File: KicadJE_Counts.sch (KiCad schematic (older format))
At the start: 105 parts, among them J101 In7, J102 Doepfer connector, J104 In6, J105 In3, J106 Out10, J107 Out11, J108 Out9, J109 Out6, SW101 Dist 6, SW102 Crush A6, SW104 Rotary_Encoder_Switch, SW105 Dist 10, U101 TL072, U102 TL072

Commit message: counter fine
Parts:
- removed A101: Arduino_Nano_v3.x, Module:Arduino_Nano, symbol KicadJE_Counts-rescue:Arduino_Nano_v3.x-MCU_Module-Kicad_Counts-rescue
- removed C119: 100n, Capacitor_SMD:C_0805_2012Metric_Pad1.15x1.40mm_HandSolder, symbol Device:C_Small
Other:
- moved on the sheet: C104, C105, C106, C107, C108, C110, C111, C112, C114, C115, C116, C117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

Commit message: Update KicadJE_Counts.sch
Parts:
- removed C114: 47n, Capacitor_SMD:C_0805_2012Metric_Pad1.15x1.40mm_HandSolder, symbol Device:C
- removed C115, C116: 100n, Capacitor_SMD:C_0805_2012Metric_Pad1.15x1.40mm_HandSolder, symbol Device:C
- removed D103: LED1, LED_THT:LED_D3.0mm, symbol Device:LED
- removed D104: LED2, LED_THT:LED_D3.0mm, symbol Device:LED
- removed D105: LED3, LED_THT:LED_D3.0mm, symbol Device:LED
- removed D107: LED4, LED_THT:LED_D3.0mm, symbol Device:LED
- removed D109: LED_Out10, LED_THT:LED_D3.0mm, symbol Device:LED
- removed D112: LED_Out11, LED_THT:LED_D3.0mm, symbol Device:LED
- removed D113: LED_Out6, LED_THT:LED_D3.0mm, symbol Device:LED
- removed D114: LED_Out9, LED_THT:LED_D3.0mm, symbol Device:LED
- removed R106, R109, R110, R113, R114, R116, R118, R121: 680R, Resistor_SMD:R_0805_2012Metric_Pad1.15x1.40mm_HandSolder, symbol Device:R
- removed R125, R126, R127: 10k, Resistor_SMD:R_0805_2012Metric_Pad1.15x1.40mm_HandSolder, symbol Device:R
- removed SW104: Rotary_Encoder_Switch, Rotary_Encoder:RotaryEncoder_Alps_EC11E-Switch_Vertical_H20mm, symbol Device:Rotary_Encoder_Switch
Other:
- note removed: "Encoder Control"
- note removed: "LED Signals"
- moved on the sheet: C104, C105, C106, C107, C108, C110, C111, C112, C117, C120, C122, C123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

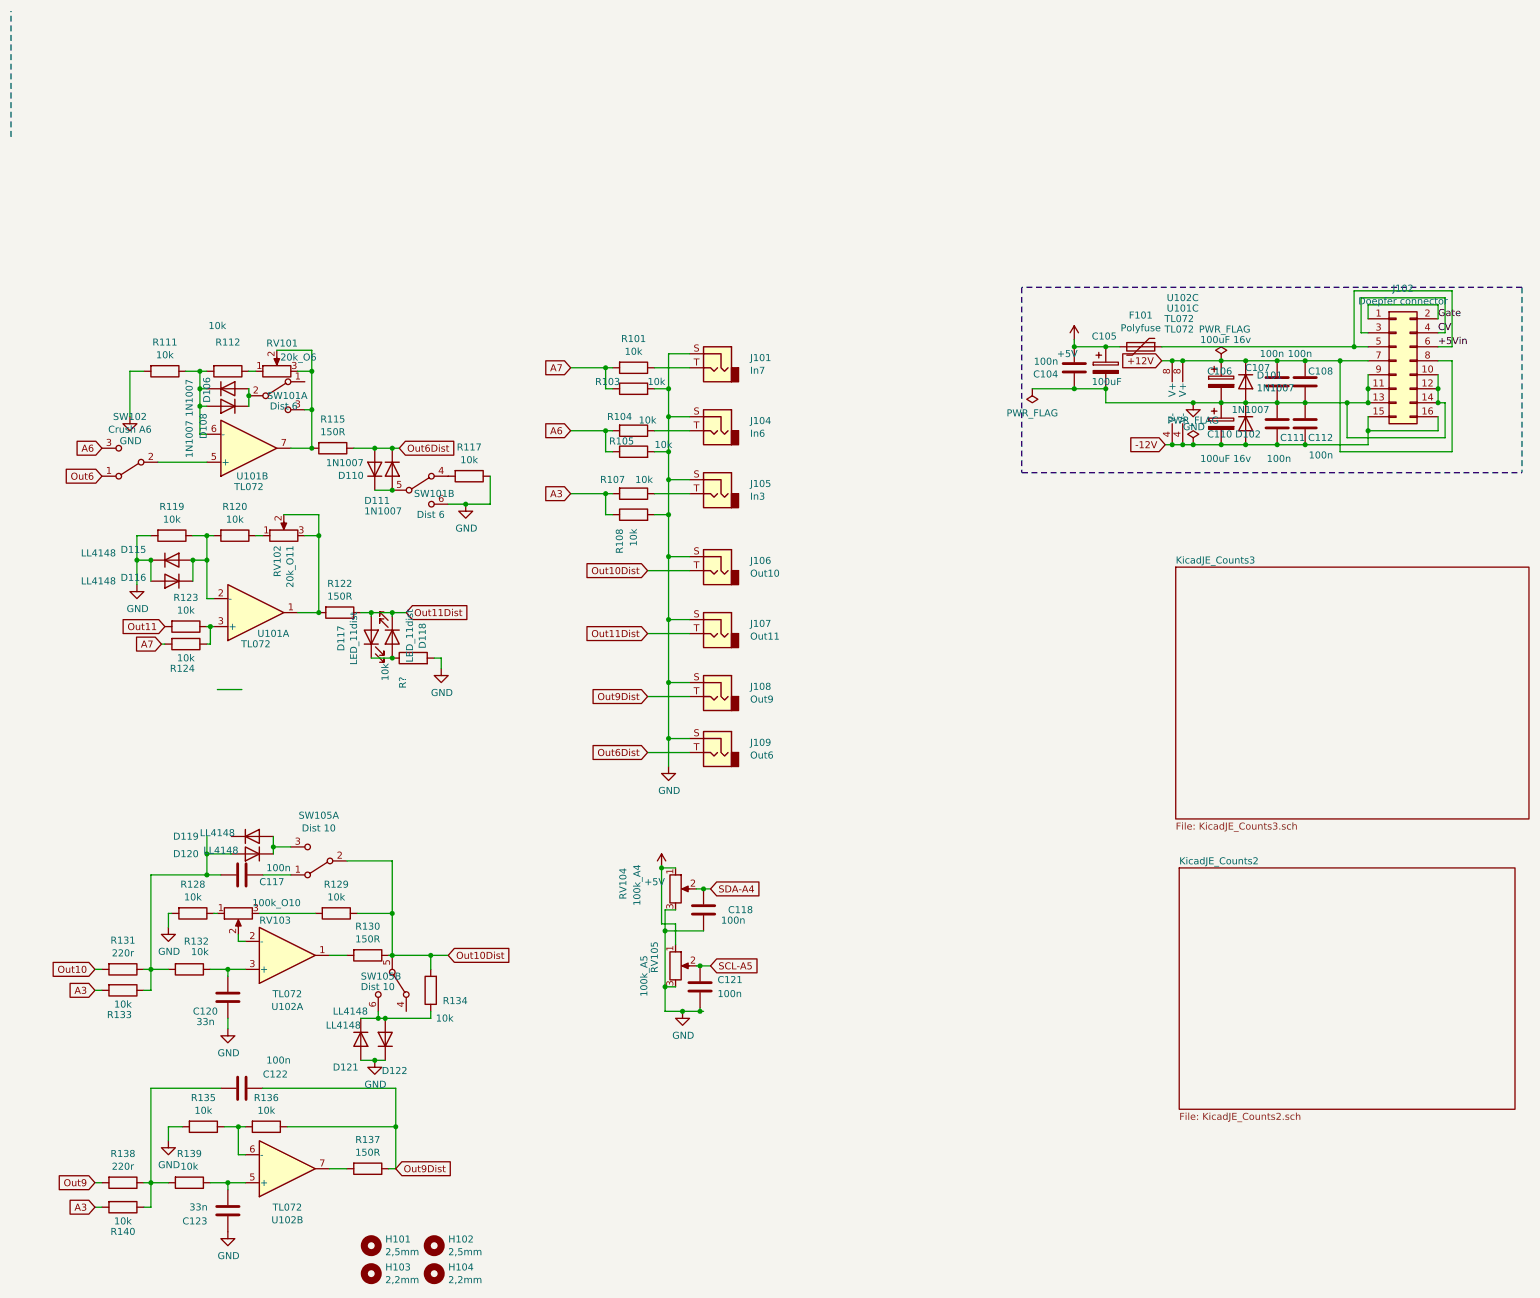
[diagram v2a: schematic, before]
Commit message: distortion added as count2
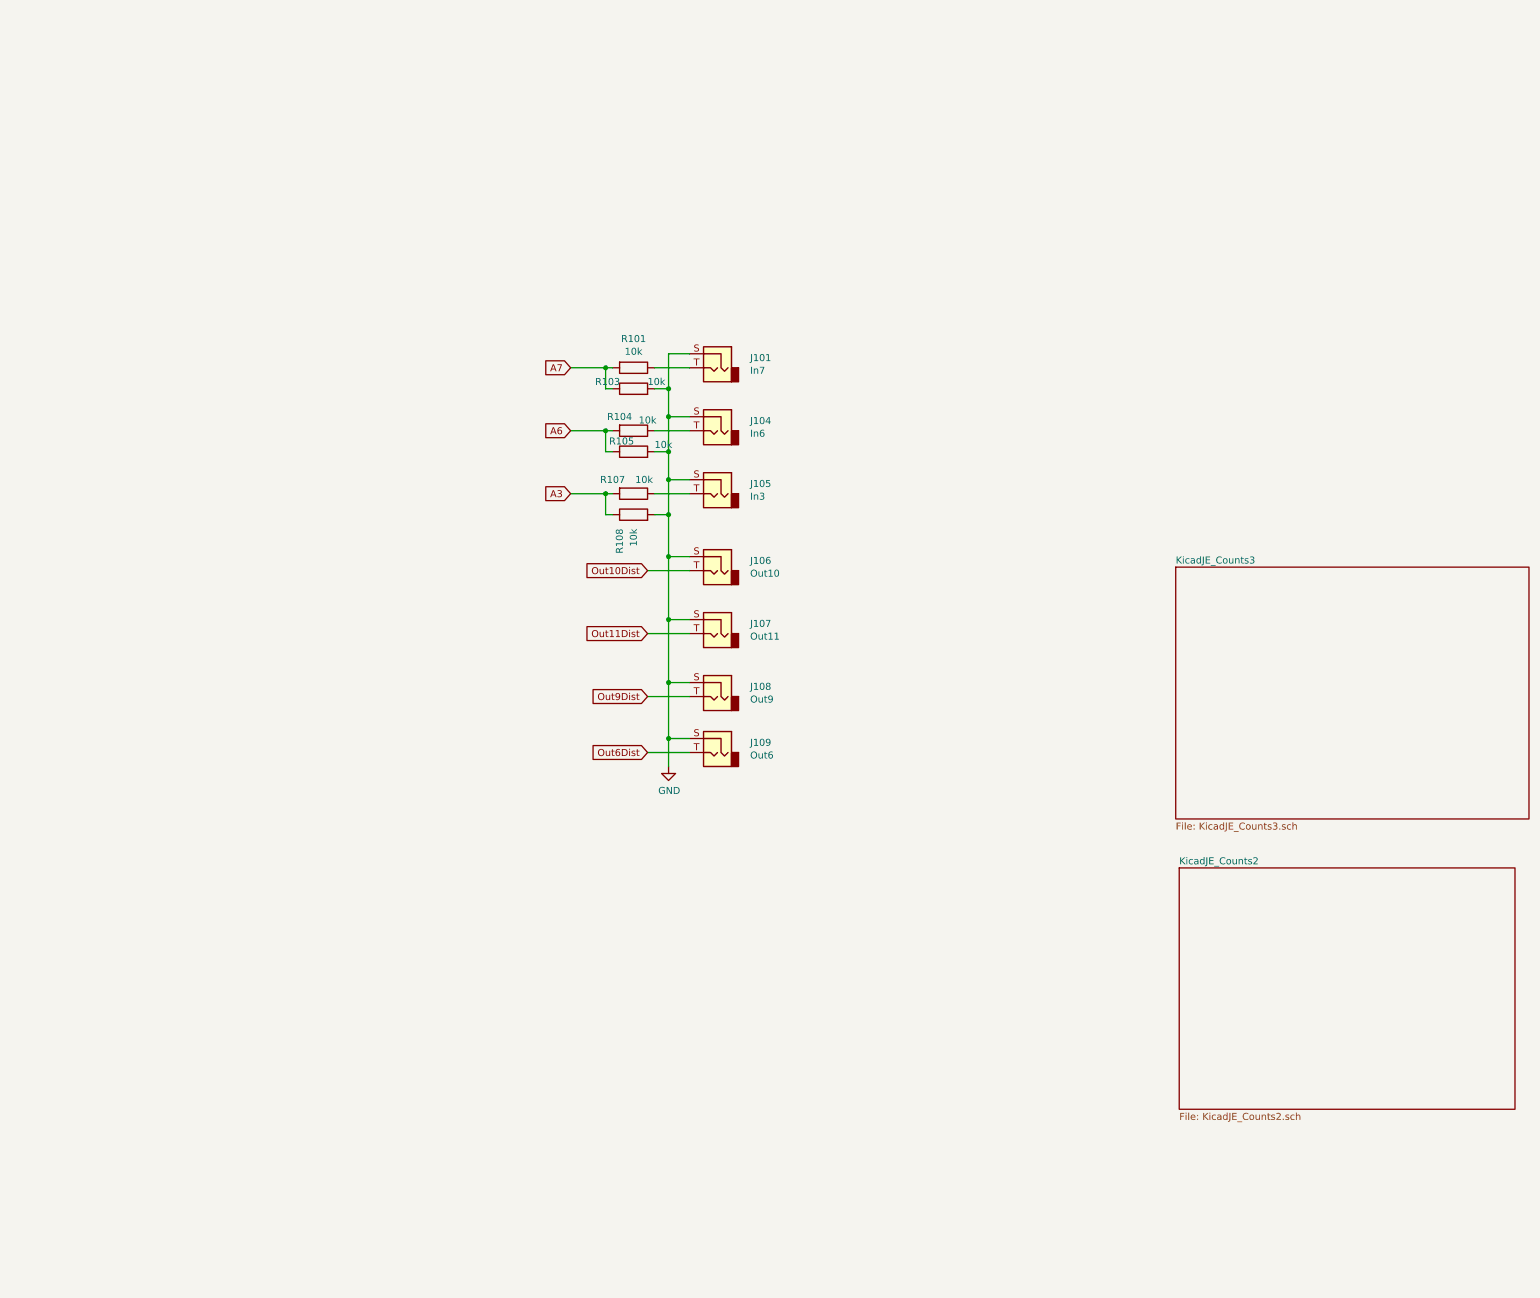
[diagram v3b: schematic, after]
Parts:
- removed C104, C107, C108, C111, C112, C117, C118, C121, C122: 100n, Capacitor_SMD:C_0805_2012Metric_Pad1.15x1.40mm_HandSolder, symbol Device:C
- removed C105: 100uF, Capacitor_THT:CP_Radial_D5.0mm_P2.50mm, symbol Device:CP
- removed C106, C110: 100uF 16v, Capacitor_THT:CP_Radial_D5.0mm_P2.50mm, symbol Device:CP
- removed C120, C123: 33n, Capacitor_SMD:C_0805_2012Metric_Pad1.15x1.40mm_HandSolder, symbol Device:C
- removed D101, D102, D106, D108: 1N1007, Diode_SMD:D_SOD-123, symbol Device:D
- removed D110, D111: 1N1007, Diode_SMD:D_0805_2012Metric_Pad1.15x1.40mm_HandSolder, symbol Device:D
- removed D115, D116, D119, D120, D121, D122: LL4148, Diode_SMD:D_MiniMELF, symbol Diode:LL4148
- removed D117: LED_11dist, LED_SMD:LED_0805_2012Metric_Pad1.15x1.40mm_HandSolder, symbol Device:LED
- removed D118: LED_11dist, Diode_SMD:D_0805_2012Metric_Pad1.15x1.40mm_HandSolder, symbol Device:LED
- removed F101: Polyfuse, Fuse:Fuse_1206_3216Metric_Pad1.42x1.75mm_HandSolder, symbol Device:Polyfuse
- removed H101, H102: 2,5mm, MountingHole:MountingHole_2.5mm_Pad_Via, symbol Mechanical:MountingHole
- removed H103: 2,2mm, MountingHole:MountingHole_2.5mm_Pad_Via, symbol Mechanical:MountingHole
- removed H104: 2,2mm, MountingHole:MountingHole_2.2mm_M2_Pad_Via, symbol Mechanical:MountingHole
- removed J102: Doepfer connector, Connector_PinSocket_2.54mm:PinSocket_2x08_P2.54mm_Vertical, symbol Connector_Generic:Conn_02x08_Odd_Even
- removed R111, R112, R117, R119, R120, R123, R124, R128, R129, R132, R133, R134, R135, R136, R139, R140, R?: 10k, Resistor_SMD:R_0805_2012Metric_Pad1.15x1.40mm_HandSolder, symbol Device:R
- removed R115, R122, R130, R137: 150R, Resistor_SMD:R_0805_2012Metric_Pad1.15x1.40mm_HandSolder, symbol Device:R
- removed R131, R138: 220r, Resistor_SMD:R_0805_2012Metric_Pad1.15x1.40mm_HandSolder, symbol Device:R
- removed RV101: 20k_O6, Potentiometer_THT:Potentiometer_China_RK09_Single_Vertical_AJ, symbol Device:R_POT
- removed RV102: 20k_O11, Potentiometer_THT:Potentiometer_China_RK09_Single_Vertical_AJ, symbol Device:R_POT
- removed RV103: 100k_O10, Potentiometer_THT:Potentiometer_China_RK09_Single_Vertical_AJ, symbol Device:R_POT
- removed RV104: 100k_A4, Potentiometer_THT:Potentiometer_China_RK09_Single_Vertical_AJ, symbol Device:R_POT
- removed RV105: 100k_A5, Potentiometer_THT:Potentiometer_China_RK09_Single_Vertical_AJ, symbol Device:R_POT
- removed SW101: Dist 6, AJ-Dropbox-Kicad:SPDTx2, symbol Switch:SW_DPDT_x2
- removed SW102: Crush A6, AJ-Dropbox-Kicad:SP1MS1, symbol Switch:SW_SPDT
- removed SW105: Dist 10, AJ-Dropbox-Kicad:SPDTx2, symbol Switch:SW_DPDT_x2
- removed U101, U102: TL072, AJ-Dropbox-Kicad:AJ_SO-8_5.3x6.2mm_P1.27mm, symbol Amplifier_Operational:TL072

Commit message: sch updates
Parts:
- renumbered J104 to J102, J105 to J103, J106 to J104, J107 to J105, J108 to J106, J109 to J107, R103 to R102, R104 to R103, R105 to R104, R107 to R105, R108 to R106
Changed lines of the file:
@@
 A6
 $Comp
-L Connector:AudioJack2 J106
+L Connector:AudioJack2 J104
 U 1 1 5C528256
 P 5375 2575
-F 0 "J106" H 5142 2646 50  0000 R CNN
+F 0 "J104" H 5142 2646 50  0000 R CNN
 F 1 "Out10" H 5142 2555 50  0000 R CNN
 F 2 "AJ-Dropbox-Kicad:PJ301SM" H 5375 2575 50  0001 C CNN
@@
 $EndComp
 $Comp
-L Connector:AudioJack2 J107
+L Connector:AudioJack2 J105
 U 1 1 5C52825C
 P 5375 3025
-F 0 "J107" H 5142 3096 50  0000 R CNN
+F 0 "J105" H 5142 3096 50  0000 R CNN
 F 1 "Out11" H 5142 3005 50  0000 R CNN
 F 2 "AJ-Dropbox-Kicad:PJ301SM" H 5375 3025 50  0001 C CNN
@@
 $EndComp
 $Comp
-L Connector:AudioJack2 J108
+L Connector:AudioJack2 J106
 U 1 1 5C528262
 P 5375 3475
-F 0 "J108" H 5142 3546 50  0000 R CNN
+F 0 "J106" H 5142 3546 50  0000 R CNN
 F 1 "Out9" H 5142 3455 50  0000 R CNN
 F 2 "AJ-Dropbox-Kicad:PJ301SM" H 5375 3475 50  0001 C CNN
@@
 $EndComp
 $Comp
-L Connector:AudioJack2 J109
+L Connector:AudioJack2 J107
 U 1 1 5C528268
 P 5375 3875
-F 0 "J109" H 5142 3946 50  0000 R CNN
+F 0 "J107" H 5142 3946 50  0000 R CNN
 F 1 "Out6" H 5142 3855 50  0000 R CNN
 F 2 "AJ-Dropbox-Kicad:PJ301SM" H 5375 3875 50  0001 C CNN
@@
 	4875 2575 5175 2575
 $Comp
-L Connector:AudioJack2 J104
+L Connector:AudioJack2 J102
 U 1 1 5C59B839
 P 5375 1575
-F 0 "J104" H 5142 1646 50  0000 R CNN
+F 0 "J102" H 5142 1646 50  0000 R CNN
 F 1 "In6" H 5142 1555 50  0000 R CNN
 F 2 "AJ-Dropbox-Kicad:PJ301SM" H 5375 1575 50  0001 C CNN
@@
 Connection ~ 5025 3775
 $Comp
-L Device:R R104
+L Device:R R103
 U 1 1 5C272108
 P 4775 1575
-F 0 "R104" V 4675 1475 50  0000 C CNN
+F 0 "R103" V 4675 1475 50  0000 C CNN
 F 1 "10k" V 4700 1675 50  0000 C CNN
 F 2 "Resistor_SMD:R_0805_2012Metric_Pad1.15x1.40mm_HandSolder" V 4705 1575 50  0001 C CNN
@@
 $EndComp
 $Comp
-L Device:R R105
+L Device:R R104
 U 1 1 5C27224E
 P 4775 1725
-F 0 "R105" V 4850 1900 50  0000 R CNN
+F 0 "R104" V 4850 1900 50  0000 R CNN
 F 1 "10k" V 4825 1575 50  0000 R CNN
 F 2 "Resistor_SMD:R_0805_2012Metric_Pad1.15x1.40mm_HandSolder" V 4705 1725 50  0001 C CNN
@@
 $EndComp
 $Comp
-L Device:R R103
+L Device:R R102
 U 1 1 5CB9F11B
 P 4775 1275
-F 0 "R103" V 4825 1550 50  0000 R CNN
+F 0 "R102" V 4825 1550 50  0000 R CNN
 F 1 "10k" V 4825 1175 50  0000 R CNN
 F 2 "Resistor_SMD:R_0805_2012Metric_Pad1.15x1.40mm_HandSolder" V 4705 1275 50  0001 C CNN
@@
 A3
 $Comp
-L Connector:AudioJack2 J105
+L Connector:AudioJack2 J103
 U 1 1 5CDF0395
 P 5375 2025
-F 0 "J105" H 5142 2096 50  0000 R CNN
+F 0 "J103" H 5142 2096 50  0000 R CNN
 F 1 "In3" H 5142 2005 50  0000 R CNN
 F 2 "AJ-Dropbox-Kicad:PJ301SM" H 5375 2025 50  0001 C CNN
@@
 	5175 1925 5025 1925
 $Comp
-L Device:R R107
+L Device:R R105
 U 1 1 5CDF039C
 P 4775 2025
-F 0 "R107" V 4675 1875 50  0000 C CNN
+F 0 "R105" V 4675 1875 50  0000 C CNN
 F 1 "10k" V 4675 2100 50  0000 C CNN
 F 2 "Resistor_SMD:R_0805_2012Metric_Pad1.15x1.40mm_HandSolder" V 4705 2025 50  0001 C CNN
@@
 $EndComp
 $Comp
-L Device:R R108
+L Device:R R106
 U 1 1 5CDF03A2
 P 4775 2175
-F 0 "R108" H 4675 2275 50  0000 R CNN
+F 0 "R106" H 4675 2275 50  0000 R CNN
 F 1 "10k" H 4675 2175 50  0000 R CNN
 F 2 "Resistor_SMD:R_0805_2012Metric_Pad1.15x1.40mm_HandSolder" V 4705 2175 50  0001 C CNN
@@
 Connection ~ 5025 1925
 $Comp
-L power:GND #PWR0107
+L power:GND #PWR0101
 U 1 1 5D3B40A8
 P 5025 3975
-F 0 "#PWR0107" H 5025 3725 50  0001 C CNN
+F 0 "#PWR0101" H 5025 3725 50  0001 C CNN
 F 1 "GND" H 5030 3802 50  0000 C CNN
 F 2 "" H 5025 3975 50  0001 C CNN

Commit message: footprint updates
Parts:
- R101, R102, R103, R104, R105, R106: footprint Resistor_SMD:R_0805_2012Metric_Pad1.15x1.40mm_HandSolder -> AJ:R_0805_AJ
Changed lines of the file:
@@
 F 0 "R103" V 4675 1475 50  0000 C CNN
 F 1 "10k" V 4700 1675 50  0000 C CNN
-F 2 "Resistor_SMD:R_0805_2012Metric_Pad1.15x1.40mm_HandSolder" V 4705 1575 50  0001 C CNN
+F 2 "AJ:R_0805_AJ" V 4705 1575 50  0001 C CNN
 F 3 "~" H 4775 1575 50  0001 C CNN
 	1    4775 1575
@@
 F 0 "R104" V 4850 1900 50  0000 R CNN
 F 1 "10k" V 4825 1575 50  0000 R CNN
-F 2 "Resistor_SMD:R_0805_2012Metric_Pad1.15x1.40mm_HandSolder" V 4705 1725 50  0001 C CNN
+F 2 "AJ:R_0805_AJ" V 4705 1725 50  0001 C CNN
 F 3 "~" H 4775 1725 50  0001 C CNN
 	1    4775 1725
@@
 F 0 "R101" V 4568 1125 50  0000 C CNN
 F 1 "10k" V 4659 1125 50  0000 C CNN
-F 2 "Resistor_SMD:R_0805_2012Metric_Pad1.15x1.40mm_HandSolder" V 4705 1125 50  0001 C CNN
+F 2 "AJ:R_0805_AJ" V 4705 1125 50  0001 C CNN
 F 3 "~" H 4775 1125 50  0001 C CNN
 	1    4775 1125
@@
 F 0 "R102" V 4825 1550 50  0000 R CNN
 F 1 "10k" V 4825 1175 50  0000 R CNN
-F 2 "Resistor_SMD:R_0805_2012Metric_Pad1.15x1.40mm_HandSolder" V 4705 1275 50  0001 C CNN
+F 2 "AJ:R_0805_AJ" V 4705 1275 50  0001 C CNN
 F 3 "~" H 4775 1275 50  0001 C CNN
 	1    4775 1275
@@
 F 0 "R105" V 4675 1875 50  0000 C CNN
 F 1 "10k" V 4675 2100 50  0000 C CNN
-F 2 "Resistor_SMD:R_0805_2012Metric_Pad1.15x1.40mm_HandSolder" V 4705 2025 50  0001 C CNN
+F 2 "AJ:R_0805_AJ" V 4705 2025 50  0001 C CNN
 F 3 "~" H 4775 2025 50  0001 C CNN
 	1    4775 2025
@@
 F 0 "R106" H 4675 2275 50  0000 R CNN
 F 1 "10k" H 4675 2175 50  0000 R CNN
-F 2 "Resistor_SMD:R_0805_2012Metric_Pad1.15x1.40mm_HandSolder" V 4705 2175 50  0001 C CNN
+F 2 "AJ:R_0805_AJ" V 4705 2175 50  0001 C CNN
 F 3 "~" H 4775 2175 50  0001 C CNN
 	1    4775 2175

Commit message: Update KicadJE_Counts.sch
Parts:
- added D? (x2): D_LED, AJ:LED_0805_2012Metric_Pad1.15x1.40mm_HandSolder, symbol Device:LED
- added R? (x2): DNP, AJ:R_0805_AJ, symbol Device:R
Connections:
- net GND: now also D?.1 (K), D?.1 (K)
- new net: D?.2 (A), R?.1 (x2)
- new net +12V: R?.2, R?.2
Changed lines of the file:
@@
 F1 "KicadJE_Counts2.sch" 50
 $EndSheet
+$Comp
+L Device:LED D?
+U 1 1 5ECDBE01
+P 10550 1650
+AR Path="/5D60ED9A/5ECDBE01" Ref="D?"  Part="1"
+AR Path="/5ECDBE01" Ref="D?"  Part="1"
+F 0 "D?" V 10589 1532 50  0000 R CNN
+F 1 "D_LED" V 10498 1532 50  0000 R CNN
+F 2 "AJ:LED_0805_2012Metric_Pad1.15x1.40mm_HandSolder" H 10550 1650 50  0001 C CNN
+F 3 "~" H 10550 1650 50  0001 C CNN
+	1    10550 1650
+	0    -1   -1   0
+$EndComp
+$Comp
+L Device:R R?
+U 1 1 5ECDBE07
+P 10550 1275
+AR Path="/5CF11B19/5ECDBE07" Ref="R?"  Part="1"
+AR Path="/5D4DB615/5ECDBE07" Ref="R?"  Part="1"
+AR Path="/5D60ED9A/5ECDBE07" Ref="R?"  Part="1"
+AR Path="/5ECDBE07" Ref="R?"  Part="1"
+F 0 "R?" V 10550 1275 50  0000 C CNN
+F 1 "DNP" V 10475 1250 50  0000 C CNN
+F 2 "AJ:R_0805_AJ" V 10480 1275 50  0001 C CNN
+F 3 "~" H 10550 1275 50  0001 C CNN
+	1    10550 1275
+	-1   0    0    1
+$EndComp
+Text GLabel 10550 1075 1    50   Input ~ 0
++12V
+$Comp
+L power:GND #PWR?
+U 1 1 5ECDBE0E
+P 10550 1900
+AR Path="/5ECDBE0E" Ref="#PWR?"  Part="1"
+AR Path="/5D60ED9A/5ECDBE0E" Ref="#PWR?"  Part="1"
+F 0 "#PWR?" H 10550 1650 50  0001 C CNN
+F 1 "GND" H 10555 1727 50  0000 C CNN
+F 2 "" H 10550 1900 50  0001 C CNN
+F 3 "" H 10550 1900 50  0001 C CNN
+	1    10550 1900
+	1    0    0    -1
+$EndComp
+Wire Wire Line
+	10550 1900 10550 1800
+Wire Wire Line
+	10550 1500 10550 1425
+Wire Wire Line
+	10550 1125 10550 1075
+$Comp
+L Device:LED D?
+U 1 1 5ECDC753
+P 10175 1650
+AR Path="/5D60ED9A/5ECDC753" Ref="D?"  Part="1"
+AR Path="/5ECDC753" Ref="D?"  Part="1"
+F 0 "D?" V 10214 1532 50  0000 R CNN
+F 1 "D_LED" V 10123 1532 50  0000 R CNN
+F 2 "AJ:LED_0805_2012Metric_Pad1.15x1.40mm_HandSolder" H 10175 1650 50  0001 C CNN
+F 3 "~" H 10175 1650 50  0001 C CNN
+	1    10175 1650
+	0    -1   -1   0
+$EndComp
+$Comp
+L Device:R R?
+U 1 1 5ECDC75D
+P 10175 1275
+AR Path="/5CF11B19/5ECDC75D" Ref="R?"  Part="1"
+AR Path="/5D4DB615/5ECDC75D" Ref="R?"  Part="1"
+AR Path="/5D60ED9A/5ECDC75D" Ref="R?"  Part="1"
+AR Path="/5ECDC75D" Ref="R?"  Part="1"
+F 0 "R?" V 10175 1275 50  0000 C CNN
+F 1 "DNP" V 10100 1250 50  0000 C CNN
+F 2 "AJ:R_0805_AJ" V 10105 1275 50  0001 C CNN
+F 3 "~" H 10175 1275 50  0001 C CNN
+	1    10175 1275
+	-1   0    0    1
+$EndComp
+Text GLabel 10175 1075 1    50   Input ~ 0
++12V
+$Comp
+L power:GND #PWR?
+U 1 1 5ECDC768
+P 10175 1900
+AR Path="/5ECDC768" Ref="#PWR?"  Part="1"
+AR Path="/5D60ED9A/5ECDC768" Ref="#PWR?"  Part="1"
+F 0 "#PWR?" H 10175 1650 50  0001 C CNN
+F 1 "GND" H 10180 1727 50  0000 C CNN
+F 2 "" H 10175 1900 50  0001 C CNN
+F 3 "" H 10175 1900 50  0001 C CNN
+	1    10175 1900
+	1    0    0    -1
+$EndComp
+Wire Wire Line
+	10175 1900 10175 1800
+Wire Wire Line
+	10175 1500 10175 1425
+Wire Wire Line
+	10175 1125 10175 1075
 $EndSCHEMATC
